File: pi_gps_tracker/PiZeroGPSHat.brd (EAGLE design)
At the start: 65 x 30 mm, 17 parts, among them IC1 24AA32ASM

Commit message: Added Jumper to WP.
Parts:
- removed TP1, TP2: TPB1,27, testpad:B1,27
- added JP1: (no value), pinhead:1X02
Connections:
- removed net N$7: IC1.7, R4.1, TP2.TP
- new net WP: IC1.7, JP1.1, R4.1
- net GND: now also JP1.2; no longer TP1.TP
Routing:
- net WP: track 0.00 -> 15.3 mm
- net N$7: track 14.5 -> 0.00 mm
- net +3V3: track 63.0 -> 65.2 mm
- added copper zone on layer 16, net GND
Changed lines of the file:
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@@
 <element name="R3" library="adafruit" package="R0805" value="9.9k" x="35.306" y="17.78" rot="R180"/>
 <element name="R4" library="adafruit" package="R0805" value="9.9k" x="35.306" y="14.478" rot="R180"/>
-<element name="TP1" library="testpad" package="B1,27" value="TPB1,27" x="39.878" y="12.954" rot="R180">
-<attribute name="TP_SIGNAL_NAME" value="" x="39.878" y="12.954" size="1.778" layer="27" rot="R180" display="off"/>
-</element>
-<element name="TP2" library="testpad" package="B1,27" value="TPB1,27" x="39.878" y="14.478">
-<attribute name="TP_SIGNAL_NAME" value="" x="39.878" y="14.478" size="1.778" layer="27" display="off"/>
-</element>
 <element name="TP3" library="testpad" package="B1,27" value="TPB1,27" x="8.128" y="12.446">
 <attribute name="TP_SIGNAL_NAME" value="" x="8.128" y="12.446" size="1.778" layer="27" display="off"/>
@@
 <attribute name="TP_SIGNAL_NAME" value="" x="4.064" y="19.05" size="1.778" layer="27" display="off"/>
 </element>
+<element name="JP1" library="pinhead" package="1X02" value="" x="41.26" y="12.98"/>
 </elements>
 <signals>
 <signal name="GND">
-<polygon width="0.3048" layer="1" rank="6">
+<polygon width="0.3048" layer="16" rank="6">
 <vertex x="0.508" y="27.178"/>
 <vertex x="2.794" y="29.464"/>
@@
 <contactref element="D1" pad="C"/>
 <contactref element="C1" pad="1"/>
-<contactref element="TP1" pad="TP"/>
+<polygon width="0.3048" layer="1" rank="6">
+<vertex x="0.508" y="27.258"/>
+<vertex x="2.794" y="29.544"/>
+<vertex x="6.858" y="29.798"/>
+<vertex x="62.23" y="29.798"/>
+<vertex x="64.516" y="27.512"/>
+<vertex x="64.516" y="2.366"/>
+<vertex x="62.738" y="0.588"/>
+<vertex x="3.302" y="0.588"/>
+<vertex x="2.032" y="1.096"/>
+<vertex x="0.508" y="3.128"/>
+</polygon>
+<contactref element="JP1" pad="2"/>
 </signal>
 <signal name="UART0_TXD">
@@
 <wire x1="34.306" y1="21.336" x2="34.306" y2="17.78" width="0.4064" layer="1"/>
 <wire x1="34.306" y1="17.78" x2="34.306" y2="14.478" width="0.4064" layer="1"/>
-<wire x1="46.2" y1="15.875" x2="46.14739375" y2="15.82239375" width="0.4064" layer="1"/>
-<wire x1="46.14739375" y1="15.82239375" x2="45.967790625" y2="15.748" width="0.4064" layer="1" curve="-44.999295"/>
-<wire x1="45.967790625" y1="15.748" x2="44.196" y2="15.748" width="0.4064" layer="1"/>
-<wire x1="44.196" y1="15.748" x2="41.98439375" y2="13.53639375" width="0.4064" layer="1"/>
-<wire x1="41.98439375" y1="13.53639375" x2="41.91" y2="13.356790625" width="0.4064" layer="1" curve="44.999295"/>
-<wire x1="41.91" y1="13.356790625" x2="41.91" y2="11.938" width="0.4064" layer="1"/>
-<wire x1="41.91" y1="11.938" x2="41.47639375" y2="11.50439375" width="0.4064" layer="1"/>
-<wire x1="41.47639375" y1="11.50439375" x2="41.296790625" y2="11.43" width="0.4064" layer="1" curve="-44.999295"/>
-<wire x1="41.296790625" y1="11.43" x2="35.814" y2="11.43" width="0.4064" layer="1"/>
-<wire x1="35.814" y1="11.43" x2="34.38039375" y2="12.86360625" width="0.4064" layer="1"/>
-<wire x1="34.38039375" y1="12.86360625" x2="34.306" y2="13.043209375" width="0.4064" layer="1" curve="-44.999295"/>
-<wire x1="34.306" y1="13.043209375" x2="34.306" y2="14.478" width="0.4064" layer="1"/>
 <wire x1="20.32" y1="17.018" x2="28.448" y2="25.146" width="0.4064" layer="1"/>
 <wire x1="13.716" y1="17.018" x2="20.32" y2="17.018" width="0.4064" layer="16"/>
@@
 <via x="20.32" y="17.018" extent="1-16" drill="0.6"/>
 <via x="13.716" y="17.018" extent="1-16" drill="0.6"/>
+<wire x1="34.306" y1="14.478" x2="34.29" y2="14.462" width="0.4064" layer="1"/>
+<wire x1="34.29" y1="14.462" x2="34.29" y2="12.15" width="0.4064" layer="1"/>
+<wire x1="34.29" y1="12.15" x2="35.43" y2="11.01" width="0.4064" layer="1"/>
+<wire x1="35.43" y1="11.01" x2="43.93" y2="11.01" width="0.4064" layer="1"/>
+<wire x1="43.93" y1="11.01" x2="44.33" y2="11.41" width="0.4064" layer="1"/>
+<wire x1="44.33" y1="11.41" x2="44.33" y2="15.22" width="0.4064" layer="1"/>
+<wire x1="44.33" y1="15.22" x2="44.985" y2="15.875" width="0.4064" layer="1"/>
+<wire x1="44.985" y1="15.875" x2="46.2" y2="15.875" width="0.4064" layer="1"/>
 </signal>
 <signal name="N$5">
@@
 <wire x1="4.974790625" y1="19.05" x2="4.064" y2="19.05" width="0.4064" layer="1"/>
 </signal>
-<signal name="N$7">
+<signal name="WP">
 <contactref element="IC1" pad="7"/>
 <contactref element="R4" pad="1"/>
-<contactref element="TP2" pad="TP"/>
-<wire x1="39.878" y1="14.478" x2="36.306" y2="14.478" width="0.4064" layer="1"/>
 <wire x1="36.306" y1="14.478" x2="38.26360625" y2="16.43560625" width="0.4064" layer="1"/>
 <wire x1="38.26360625" y1="16.43560625" x2="38.443209375" y2="16.51" width="0.4064" layer="1" curve="-44.999295"/>
@@
 <wire x1="43.74060625" y1="17.07060625" x2="43.920209375" y2="17.145" width="0.4064" layer="1" curve="-44.999295"/>
 <wire x1="43.920209375" y1="17.145" x2="46.2" y2="17.145" width="0.4064" layer="1"/>
+<contactref element="JP1" pad="1"/>
+<wire x1="36.306" y1="14.478" x2="37.804" y2="12.98" width="0.4064" layer="1"/>
+<wire x1="37.804" y1="12.98" x2="39.99" y2="12.98" width="0.4064" layer="1"/>
 </signal>
 </signals>

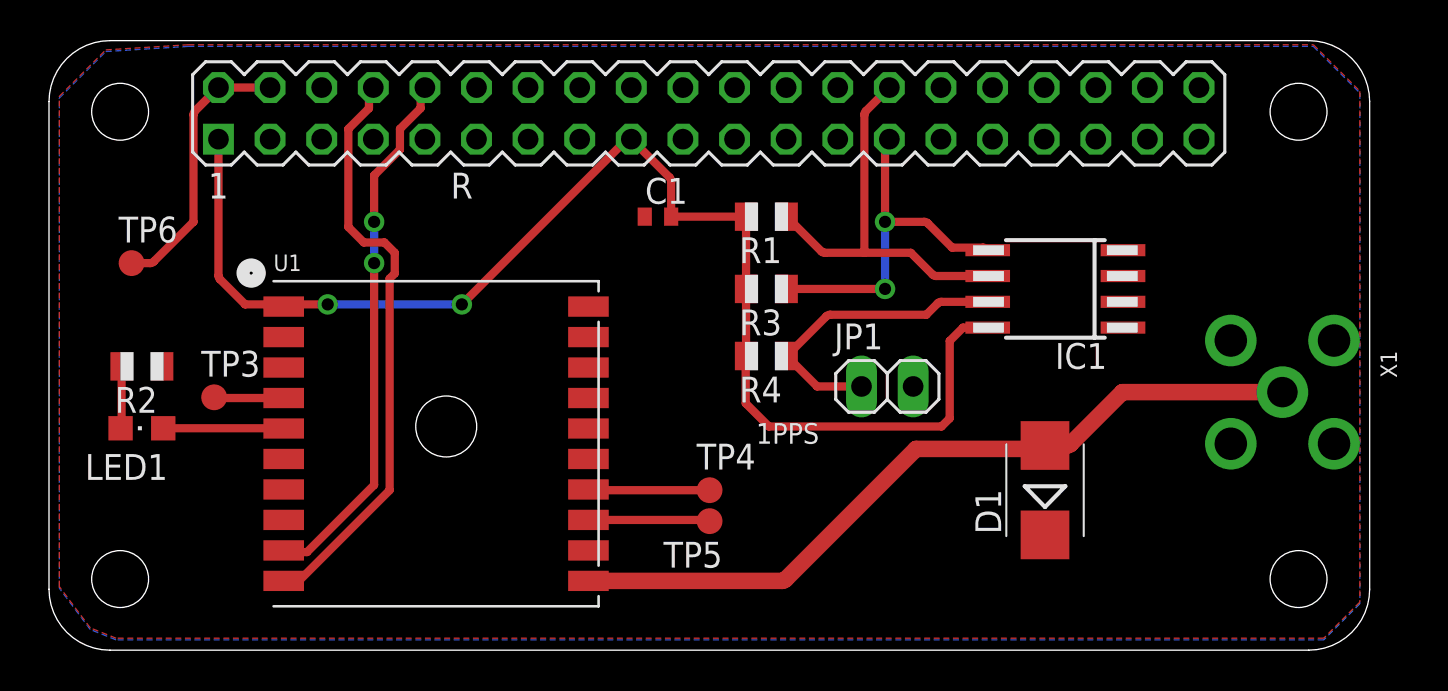
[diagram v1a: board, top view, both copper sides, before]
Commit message: V2 of the GPS hat to add LEDs for status indicators
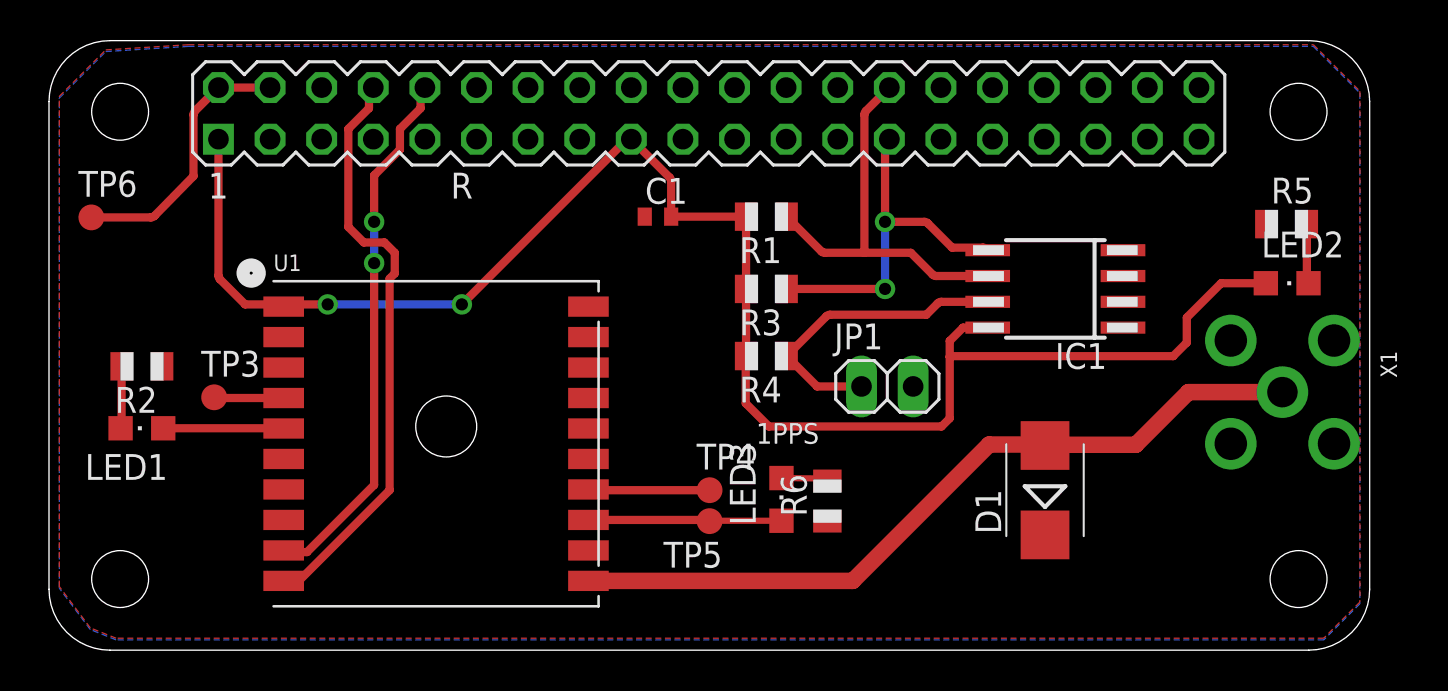
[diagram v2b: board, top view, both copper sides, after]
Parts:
- added LED2, LED3: 1, adafruit:CHIPLED_0805
- added R5, R6: 470, adafruit:R0805
- moved TP6 3.00 mm to (2.08, 21.3)
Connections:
- removed net N$3: TP5.TP, U1.P$13
- new net 1PPS: LED3.A, TP5.TP, U1.P$13
- new net N$7: LED2.C, R5.2
- new net N$8: LED3.C, R6.2
- net +3V3: now also LED2.A
- net GND: now also R5.1, R6.1
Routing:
- net +3V3: track 65.2 -> 83.0 mm
- net 1PPS: track 0.00 -> 9.52 mm
- net N$3: track 5.97 -> 0.00 mm
- net N$7: track 0.00 -> 2.94 mm
- net N$8: track 0.00 -> 2.32 mm
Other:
- board text added: "PiGPSHat V2"
- board text removed: "Brandon Smith"
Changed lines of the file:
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@@
 <?xml version="1.0" encoding="utf-8"?>
 <!DOCTYPE eagle SYSTEM "eagle.dtd">
-<eagle version="7.3.0">
+<eagle version="7.5.0">
 <drawing>
 <settings>
@@
 <plain>
 <text x="34.798" y="10.16" size="1.016" layer="25">1PPS</text>
-<text x="40.386" y="1.524" size="1.778" layer="51">Brandon Smith</text>
+<text x="45.846" y="1.186" size="1.4224" layer="51">PiGPSHat V2</text>
 </plain>
 <attributes>
@@
 <attribute name="TP_SIGNAL_NAME" value="" x="32.512" y="6.35" size="1.778" layer="27" rot="R180" display="off"/>
 </element>
-<element name="TP6" library="testpad" package="B1,27" value="TPB1,27" x="4.064" y="19.05">
-<attribute name="TP_SIGNAL_NAME" value="" x="4.064" y="19.05" size="1.778" layer="27" display="off"/>
+<element name="TP6" library="testpad" package="B1,27" value="TPB1,27" x="2.084" y="21.3">
+<attribute name="TP_SIGNAL_NAME" value="" x="2.084" y="21.3" size="1.778" layer="27" display="off"/>
 </element>
 <element name="JP1" library="pinhead" package="1X02" value="" x="41.26" y="12.98"/>
+<element name="LED2" library="adafruit" package="CHIPLED_0805" value="1" x="60.94" y="18.06" rot="R270"/>
+<element name="R5" library="adafruit" package="R0805" value="470" x="60.91" y="20.97"/>
+<element name="LED3" library="adafruit" package="CHIPLED_0805" value="1" x="36.05" y="7.42"/>
+<element name="R6" library="adafruit" package="R0805" value="470" x="38.31" y="7.34" rot="R90"/>
 </elements>
 <signals>
@@
 </polygon>
 <contactref element="JP1" pad="2"/>
+<contactref element="R5" pad="1"/>
+<contactref element="R6" pad="1"/>
 </signal>
 <signal name="UART0_TXD">
@@
 <wire x1="3.572" y1="11.042709375" x2="3.572" y2="13.97" width="0.4064" layer="1"/>
 </signal>
-<signal name="N$3">
+<signal name="1PPS">
 <contactref element="U1" pad="P$13"/>
 <contactref element="TP5" pad="TP"/>
 <wire x1="32.512" y1="6.35" x2="32.367146875" y2="6.41" width="0.4064" layer="1" curve="45"/>
 <wire x1="32.367146875" y1="6.41" x2="26.55" y2="6.41" width="0.4064" layer="1"/>
+<contactref element="LED3" pad="A"/>
+<wire x1="36.05" y1="6.37" x2="32.532" y2="6.37" width="0.3048" layer="1"/>
+<wire x1="32.532" y1="6.37" x2="32.512" y2="6.35" width="0.3048" layer="1"/>
 </signal>
 <signal name="N$4">
@@
 <contactref element="X1" pad="ANTENNA"/>
 <contactref element="D1" pad="A"/>
-<wire x1="60.706" y1="12.7" x2="52.832" y2="12.7" width="0.8128" layer="1"/>
-<wire x1="52.832" y1="12.7" x2="50.28039375" y2="10.14839375" width="0.8128" layer="1"/>
-<wire x1="50.28039375" y1="10.14839375" x2="50.100790625" y2="10.074" width="0.8128" layer="1" curve="-44.999295"/>
-<wire x1="50.100790625" y1="10.074" x2="49.022" y2="10.074" width="0.8128" layer="1"/>
-<wire x1="49.022" y1="10.074" x2="48.92839375" y2="9.98039375" width="0.8128" layer="1"/>
-<wire x1="48.92839375" y1="9.98039375" x2="48.748790625" y2="9.906" width="0.8128" layer="1" curve="-44.999295"/>
-<wire x1="48.748790625" y1="9.906" x2="42.672" y2="9.906" width="0.8128" layer="1"/>
-<wire x1="42.672" y1="9.906" x2="36.25039375" y2="3.48439375" width="0.8128" layer="1"/>
-<wire x1="36.25039375" y1="3.48439375" x2="36.070790625" y2="3.41" width="0.8128" layer="1" curve="-44.999295"/>
-<wire x1="36.070790625" y1="3.41" x2="26.55" y2="3.41" width="0.8128" layer="1"/>
+<wire x1="26.55" y1="3.41" x2="39.56" y2="3.41" width="0.8128" layer="1"/>
+<wire x1="39.56" y1="3.41" x2="46.27" y2="10.12" width="0.8128" layer="1"/>
+<wire x1="46.27" y1="10.12" x2="48.976" y2="10.12" width="0.8128" layer="1"/>
+<wire x1="48.976" y1="10.12" x2="49.022" y2="10.074" width="0.8128" layer="1"/>
+<wire x1="60.706" y1="12.7" x2="56.08" y2="12.7" width="0.8128" layer="1"/>
+<wire x1="56.08" y1="12.7" x2="53.49" y2="10.11" width="0.8128" layer="1"/>
+<wire x1="53.49" y1="10.11" x2="49.058" y2="10.11" width="0.8128" layer="1"/>
+<wire x1="49.058" y1="10.11" x2="49.022" y2="10.074" width="0.8128" layer="1"/>
 </signal>
 <signal name="+3V3">
@@
 <wire x1="35.43" y1="11.01" x2="43.93" y2="11.01" width="0.4064" layer="1"/>
 <wire x1="43.93" y1="11.01" x2="44.33" y2="11.41" width="0.4064" layer="1"/>
-<wire x1="44.33" y1="11.41" x2="44.33" y2="15.22" width="0.4064" layer="1"/>
+<wire x1="44.33" y1="11.41" x2="44.33" y2="14.44" width="0.4064" layer="1"/>
+<wire x1="44.33" y1="14.44" x2="44.33" y2="15.22" width="0.4064" layer="1"/>
 <wire x1="44.33" y1="15.22" x2="44.985" y2="15.875" width="0.4064" layer="1"/>
 <wire x1="44.985" y1="15.875" x2="46.2" y2="15.875" width="0.4064" layer="1"/>
+<contactref element="LED2" pad="A"/>
+<wire x1="59.89" y1="18.06" x2="57.69" y2="18.06" width="0.4064" layer="1"/>
+<wire x1="57.69" y1="18.06" x2="56" y2="16.37" width="0.4064" layer="1"/>
+<wire x1="56" y1="16.37" x2="56" y2="15.14" width="0.4064" layer="1"/>
+<wire x1="56" y1="15.14" x2="55.33" y2="14.47" width="0.4064" layer="1"/>
+<wire x1="55.33" y1="14.47" x2="44.36" y2="14.47" width="0.4064" layer="1"/>
+<wire x1="44.36" y1="14.47" x2="44.33" y2="14.44" width="0.4064" layer="1"/>
 </signal>
 <signal name="N$5">
@@
 <wire x1="8.34" y1="27.69" x2="7.18639375" y2="26.53639375" width="0.4064" layer="1"/>
 <wire x1="7.18639375" y1="26.53639375" x2="7.112" y2="26.356790625" width="0.4064" layer="1" curve="44.999295"/>
-<wire x1="7.112" y1="26.356790625" x2="7.112" y2="21.082" width="0.4064" layer="1"/>
-<wire x1="7.112" y1="21.082" x2="5.15439375" y2="19.12439375" width="0.4064" layer="1"/>
-<wire x1="5.15439375" y1="19.12439375" x2="4.974790625" y2="19.05" width="0.4064" layer="1" curve="-44.999295"/>
-<wire x1="4.974790625" y1="19.05" x2="4.064" y2="19.05" width="0.4064" layer="1"/>
+<wire x1="7.112" y1="26.356790625" x2="7.112" y2="23.332" width="0.4064" layer="1"/>
+<wire x1="7.112" y1="23.332" x2="5.19439375" y2="21.37439375" width="0.4064" layer="1"/>
+<wire x1="5.19439375" y1="21.37439375" x2="5.014790625" y2="21.3" width="0.4064" layer="1" curve="-44.999295"/>
+<wire x1="5.014790625" y1="21.3" x2="2.084" y2="21.3" width="0.4064" layer="1"/>
 </signal>
 <signal name="WP">
@@
 <wire x1="37.804" y1="12.98" x2="39.99" y2="12.98" width="0.4064" layer="1"/>
 </signal>
+<signal name="N$7">
+<contactref element="LED2" pad="C"/>
+<contactref element="R5" pad="2"/>
+<wire x1="61.91" y1="20.97" x2="61.91" y2="18.14" width="0.4064" layer="1"/>
+<wire x1="61.91" y1="18.14" x2="61.99" y2="18.06" width="0.4064" layer="1"/>
+</signal>
+<signal name="N$8">
+<contactref element="LED3" pad="C"/>
+<contactref element="R6" pad="2"/>
+<wire x1="36.05" y1="8.47" x2="38.23" y2="8.45" width="0.3048" layer="1"/>
+<wire x1="38.23" y1="8.45" x2="38.31" y2="8.34" width="0.3048" layer="1"/>
+</signal>
 </signals>

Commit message: V3 moved all the LEDs to the same location.
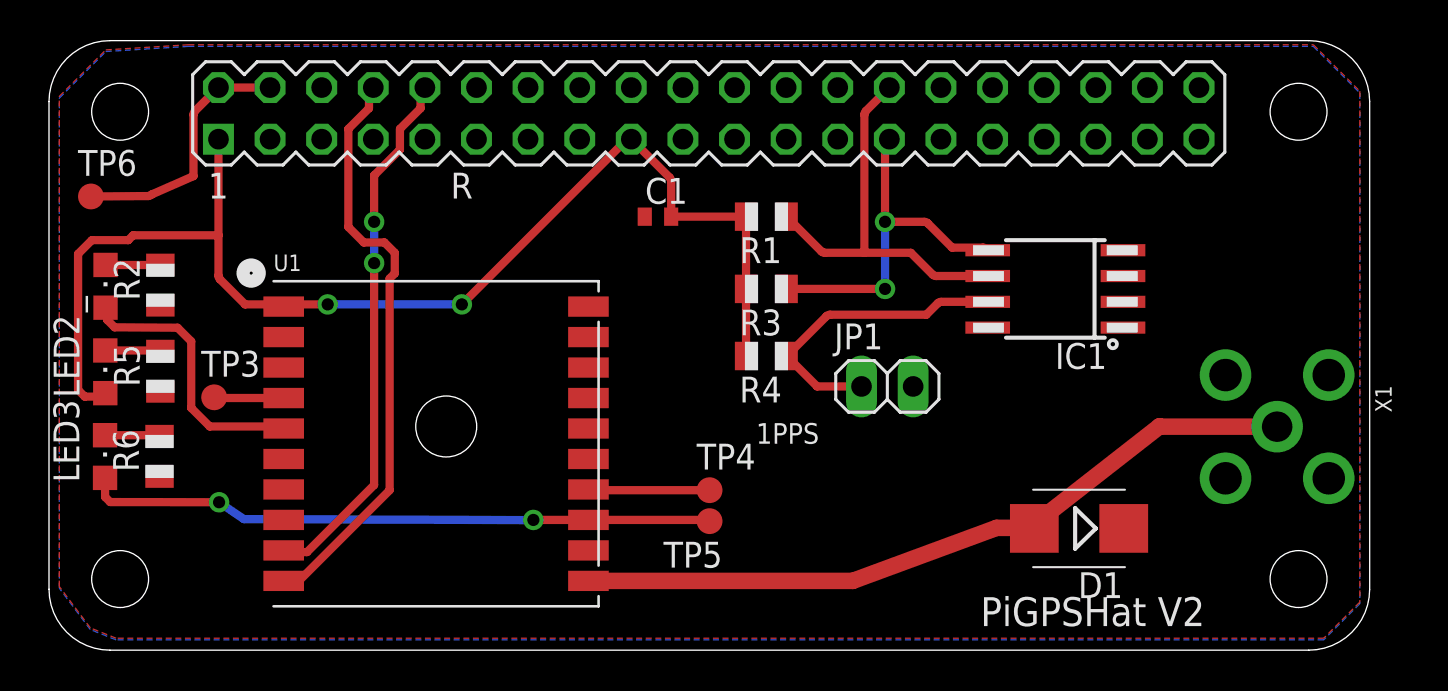
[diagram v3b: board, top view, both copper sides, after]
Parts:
- removed LED1: 1, adafruit:CHIPLED_0805
- added _: 1, adafruit:CHIPLED_0805
- moved LED2 58.3 mm to (2.77, 13.7), turned to 0 degrees
- moved R5 55.9 mm to (5.48, 13.7), turned to 90 degrees
- moved LED3 33.4 mm to (2.76, 9.53)
- moved R6 32.9 mm to (5.44, 9.54)
- moved R2 4.10 mm to (5.48, 18.0), turned to 90 degrees
- moved D1 2.52 mm to (50.7, 5.99), turned to 180 degrees
- moved X1 1.72 mm to (60.4, 11.0)
- moved TP6 1.03 mm to (2.06, 22.3)
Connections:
- net N$1: now also _.A; no longer LED1.A
- net N$2: now also _.C; no longer LED1.C
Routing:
- net 1PPS: track 9.52 -> 31.1 mm, vias 0 -> 2
- net +3V3: track 83.0 -> 61.8 mm
- net N$1: track 5.93 -> 13.4 mm
- net N$6: track 38.0 -> 36.3 mm
- net +5V: track 13.3 -> 12.6 mm

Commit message: New Board and SCAD
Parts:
- removed D1: ES2D, diode:SMB
- removed LED2, LED3, _: 1, adafruit:CHIPLED_0805
- removed TP6: TPB1,27, testpad:B1,27
- added 1PPS, 3V3, FIX, LED1: 1, adafruit:CHIPLED_0805
- added R7: 470, adafruit:R0402
- R1, R3: value 9.9k -> 3.9k; device adafruit:R0805 -> adafruit:R0402
- R2, R5, R6: device adafruit:R0805 -> adafruit:R0402
- R4: value 9.9k -> 1.2k; device adafruit:R0805 -> adafruit:R0402
- moved TP3 53.6 mm to (61.1, 20.6)
- moved TP4 30.4 mm to (61.1, 18.2)
- moved TP5 30.2 mm to (61.1, 16.1), turned to 0 degrees
- moved R5 4.98 mm to (6.38, 18.6)
- moved R2 4.20 mm to (6.38, 13.9)
- moved R6 1.00 mm to (6.44, 9.54)
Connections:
- removed net +5V: R.2, R.4, TP6.TP
- new net GP2: R.3
- new net GP3: R.5
- new net GP4: LED1.A, R.7
- new net N$3: LED1.C, R7.2
- net +3V3: now also 3V3.A; no longer LED2.A
- net 1PPS: now also 1PPS.A; no longer LED3.A
- net GND: now also R7.1; no longer D1.C
- net N$1: now also FIX.A; no longer _.A
- net N$2: now also FIX.C; no longer _.C
- net N$6: no longer D1.A
- net N$7: now also 3V3.C; no longer LED2.C
- net N$8: now also 1PPS.C; no longer LED3.C
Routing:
- net N$5: track 3.43 -> 54.2 mm, vias 0 -> 2
- net N$4: track 5.97 -> 38.9 mm
- net 1PPS: track 31.1 -> 62.0 mm
- net +5V: track 12.6 -> 0.00 mm
- net GP4: track 0.00 -> 9.88 mm, vias 0 -> 1
- net +3V3: track 61.8 -> 71.1 mm, vias 2 -> 1
- net N$1: track 13.4 -> 8.93 mm
- net N$3: track 0.00 -> 4.14 mm
- net N$6: track 36.3 -> 37.0 mm
- net N$7: track 2.73 -> 3.38 mm
- net WP: track 15.3 -> 15.8 mm
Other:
- board text removed: "1PPS"
